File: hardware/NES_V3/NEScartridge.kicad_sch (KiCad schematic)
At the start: 39 parts, among them J1 Conn_02x36_Top_Bottom, U1 TXS0108EPW, U10 TXS0108EPW, U11 TXS0108EPW, U2 TXS0108EPW, U5 TXS0108EPW, U6 TXS0108EPW, U7 TXS0108EPW, U8 TXS0108EPW, U9 TXS0108EPW

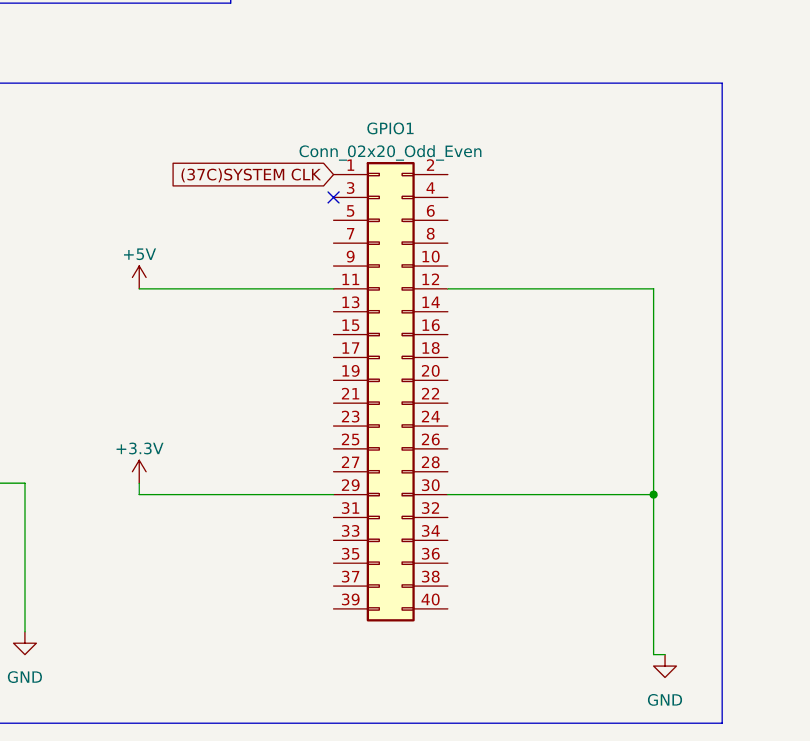
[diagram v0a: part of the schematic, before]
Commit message: Update on the V3 of the cartridge
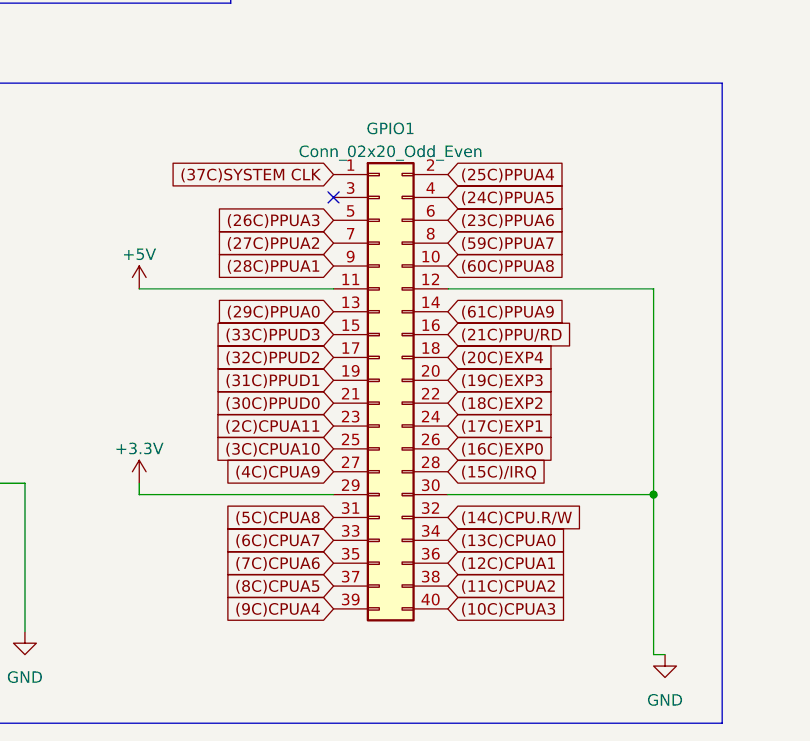
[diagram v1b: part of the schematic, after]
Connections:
- net (10C)CPUA3: now also GPIO1.40 (Pin_40)
- net (11C)CPUA2: now also GPIO1.38 (Pin_38)
- net (12C)CPUA1: now also GPIO1.36 (Pin_36)
- net (13C)CPUA0: now also GPIO1.34 (Pin_34)
- net (14C)CPU.R/W: now also GPIO1.32 (Pin_32)
- net (15C)/IRQ: now also GPIO1.28 (Pin_28)
- net (16C)EXP0: now also GPIO1.26 (Pin_26)
- net (17C)EXP1: now also GPIO1.24 (Pin_24)
- net (18C)EXP2: now also GPIO1.22 (Pin_22)
- net (19C)EXP3: now also GPIO1.20 (Pin_20)
- net (20C)EXP4: now also GPIO1.18 (Pin_18)
- net (21C)PPU/RD: now also GPIO1.16 (Pin_16)
- net (23C)PPUA6: now also GPIO1.6 (Pin_6)
- net (24C)PPUA5: now also GPIO1.4 (Pin_4)
- net (25C)PPUA4: now also GPIO1.2 (Pin_2)
- net (26C)PPUA3: now also GPIO1.5 (Pin_5)
- net (27C)PPUA2: now also GPIO1.7 (Pin_7)
- net (28C)PPUA1: now also GPIO1.9 (Pin_9)
- net (29C)PPUA0: now also GPIO1.13 (Pin_13)
- net (2C)CPUA11: now also GPIO1.23 (Pin_23)
- net (30C)PPUD0: now also GPIO1.21 (Pin_21)
- net (31C)PPUD1: now also GPIO1.19 (Pin_19)
- net (32C)PPUD2: now also GPIO1.17 (Pin_17)
- net (33C)PPUD3: now also GPIO1.15 (Pin_15)
- net (3C)CPUA10: now also GPIO1.25 (Pin_25)
- net (4C)CPUA9: now also GPIO1.27 (Pin_27)
- net (59C)PPUA7: now also GPIO1.8 (Pin_8)
- net (5C)CPUA8: now also GPIO1.31 (Pin_31)
- net (60C)PPUA8: now also GPIO1.10 (Pin_10)
- net (61C)PPUA9: now also GPIO1.14 (Pin_14)
- net (6C)CPUA7: now also GPIO1.33 (Pin_33)
- net (7C)CPUA6: now also GPIO1.35 (Pin_35)
- net (8C)CPUA5: now also GPIO1.37 (Pin_37)
- net (9C)CPUA4: now also GPIO1.39 (Pin_39)

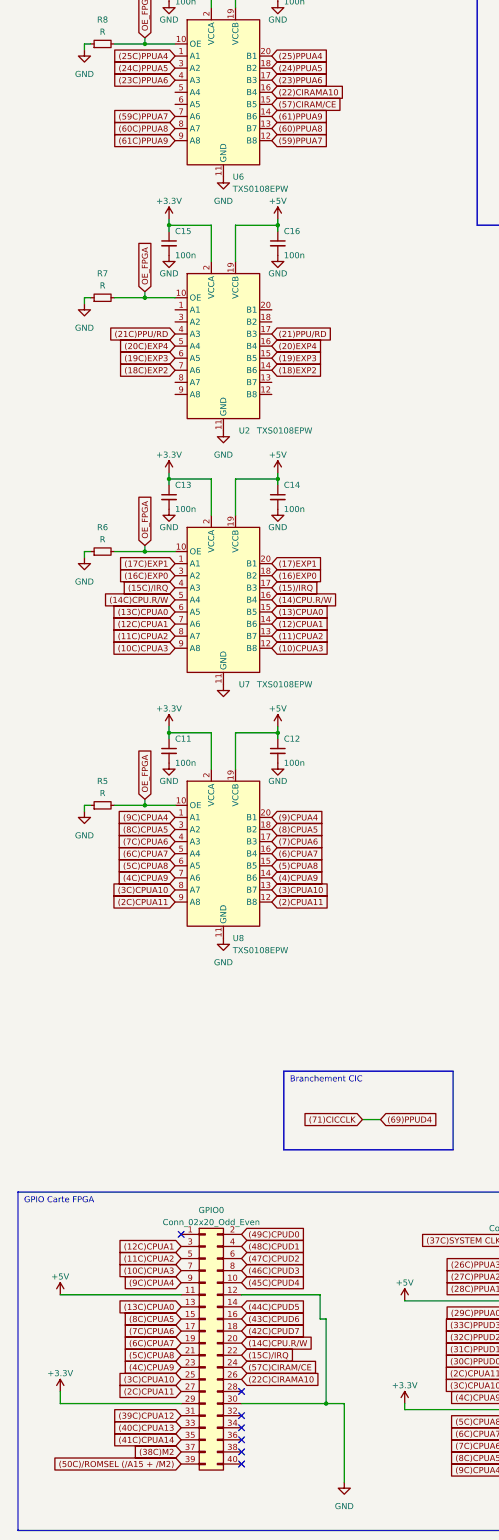
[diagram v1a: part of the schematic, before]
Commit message: Update on the V3 of the cartridge - PCB
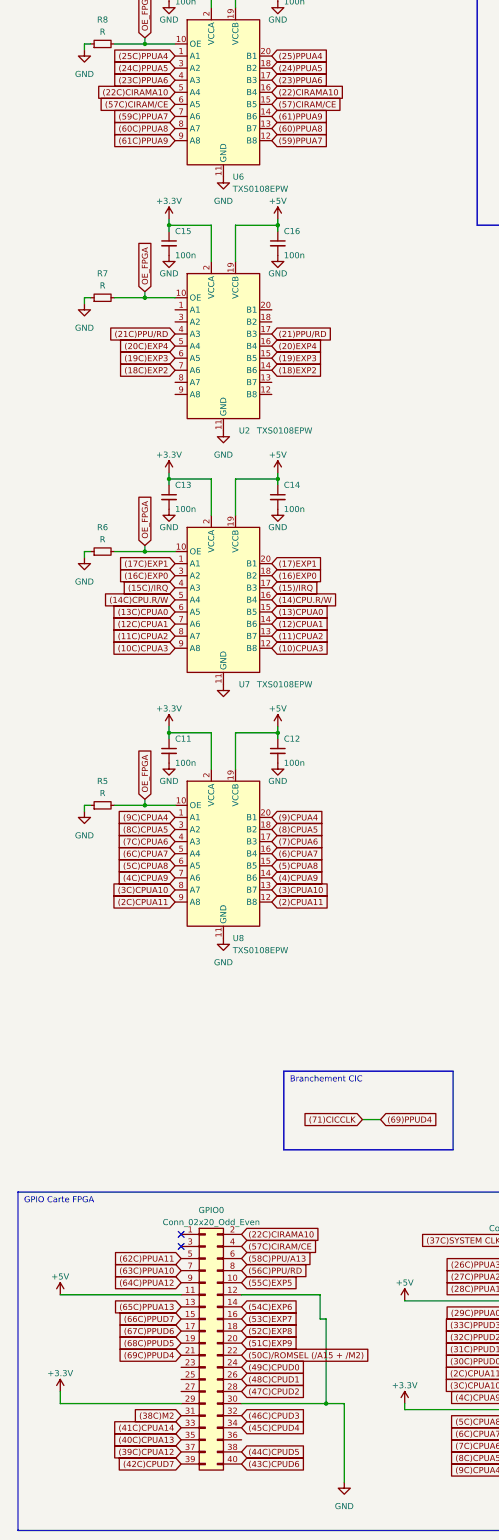
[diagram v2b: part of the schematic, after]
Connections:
- net (10C)CPUA3: no longer GPIO0.7 (Pin_7)
- net (11C)CPUA2: no longer GPIO0.5 (Pin_5)
- net (12C)CPUA1: no longer GPIO0.3 (Pin_3)
- net (13C)CPUA0: no longer GPIO0.13 (Pin_13)
- net (14C)CPU.R/W: no longer GPIO0.20 (Pin_20)
- net (15C)/IRQ: no longer GPIO0.22 (Pin_22)
- net (22C)CIRAMA10: now also GPIO0.2 (Pin_2), U6.5 (A4); no longer GPIO0.26 (Pin_26)
- net (2C)CPUA11: no longer GPIO0.27 (Pin_27)
- net (38C)M2: now also GPIO0.31 (Pin_31); no longer GPIO0.37 (Pin_37)
- net (39C)CPUA12: now also GPIO0.37 (Pin_37); no longer GPIO0.31 (Pin_31)
- net (3C)CPUA10: no longer GPIO0.25 (Pin_25)
- net (40C)CPUA13: now also GPIO0.35 (Pin_35); no longer GPIO0.33 (Pin_33)
- net (41C)CPUA14: now also GPIO0.33 (Pin_33); no longer GPIO0.35 (Pin_35)
- net (42C)CPUD7: now also GPIO0.39 (Pin_39); no longer GPIO0.18 (Pin_18)
- net (43C)CPUD6: now also GPIO0.40 (Pin_40); no longer GPIO0.16 (Pin_16)
- net (44C)CPUD5: now also GPIO0.38 (Pin_38); no longer GPIO0.14 (Pin_14)
- net (45C)CPUD4: now also GPIO0.34 (Pin_34); no longer GPIO0.10 (Pin_10)
- net (46C)CPUD3: now also GPIO0.32 (Pin_32); no longer GPIO0.8 (Pin_8)
- net (47C)CPUD2: now also GPIO0.28 (Pin_28); no longer GPIO0.6 (Pin_6)
- net (48C)CPUD1: now also GPIO0.26 (Pin_26); no longer GPIO0.4 (Pin_4)
- net (49C)CPUD0: now also GPIO0.24 (Pin_24); no longer GPIO0.2 (Pin_2)
- net (4C)CPUA9: no longer GPIO0.23 (Pin_23)
- net (50C)/ROMSEL (/A15 + /M2): now also GPIO0.22 (Pin_22); no longer GPIO0.39 (Pin_39)
- net (51C)EXP9: now also GPIO0.20 (Pin_20)
- net (52C)EXP8: now also GPIO0.18 (Pin_18)
- net (53C)EXP7: now also GPIO0.16 (Pin_16)
- net (54C)EXP6: now also GPIO0.14 (Pin_14)
- net (55C)EXP5: now also GPIO0.10 (Pin_10)
- net (56C)PPU/RD: now also GPIO0.8 (Pin_8)
- net (57C)CIRAM/CE: now also GPIO0.4 (Pin_4), U6.6 (A5); no longer GPIO0.24 (Pin_24)
- net (58C)PPU/A13: now also GPIO0.6 (Pin_6)
- net (5C)CPUA8: no longer GPIO0.21 (Pin_21)
- net (62C)PPUA11: now also GPIO0.5 (Pin_5)
- net (63C)PPUA10: now also GPIO0.7 (Pin_7)
- net (64C)PPUA12: now also GPIO0.9 (Pin_9)
- net (65C)PPUA13: now also GPIO0.13 (Pin_13)
- net (66C)PPUD7: now also GPIO0.15 (Pin_15)
- net (67C)PPUD6: now also GPIO0.17 (Pin_17)
- net (68C)PPUD5: now also GPIO0.19 (Pin_19)
- net (69C)PPUD4: now also GPIO0.21 (Pin_21)
- net (6C)CPUA7: no longer GPIO0.19 (Pin_19)
- net (7C)CPUA6: no longer GPIO0.17 (Pin_17)
- net (8C)CPUA5: no longer GPIO0.15 (Pin_15)
- net (9C)CPUA4: no longer GPIO0.9 (Pin_9)
- no-connect marks 8 -> 3

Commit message: Corrected DRC errors/warning on V5
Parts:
- R10, R11, R12, R13, R5, R6, R7, R8, R9: value R -> 10k
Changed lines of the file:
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@@
     (stroke (width 0) (type default))
   )
-  (polyline (pts (xy 74.93 322.58) (xy 74.93 306.07))
+  (polyline (pts (xy 19.05 328.93) (xy 19.05 312.42))
     (stroke (width 0) (type default))
   )
@@
     (stroke (width 0) (type default))
   )
-  (polyline (pts (xy 74.93 306.07) (xy 110.49 306.07))
+  (polyline (pts (xy 19.05 312.42) (xy 54.61 312.42))
     (stroke (width 0) (type default))
   )
@@
     (stroke (width 0) (type default))
   )
-  (polyline (pts (xy 110.49 322.58) (xy 74.93 322.58))
+  (polyline (pts (xy 54.61 328.93) (xy 19.05 328.93))
     (stroke (width 0) (type default))
   )
@@
     (stroke (width 0) (type default))
   )
-  (wire (pts (xy 91.44 316.23) (xy 95.25 316.23))
+  (wire (pts (xy 35.56 322.58) (xy 39.37 322.58))
     (stroke (width 0) (type default))
   )
@@
     (stroke (width 0) (type default))
   )
-  (polyline (pts (xy 74.93 306.07) (xy 74.93 306.07))
+  (polyline (pts (xy 19.05 312.42) (xy 19.05 312.42))
     (stroke (width 0) (type default))
   )
@@
     (stroke (width 0) (type default))
   )
-  (polyline (pts (xy 110.49 306.07) (xy 110.49 322.58))
+  (polyline (pts (xy 54.61 312.42) (xy 54.61 328.93))
     (stroke (width 0) (type default))
   )
@@
     (effects (font (size 1.27 1.27)) (justify left bottom))
   )
-  (text "Branchement CIC\n" (at 76.2 308.61 0)
+  (text "Branchement CIC\n" (at 20.32 314.96 0)
     (effects (font (size 1.27 1.27)) (justify left bottom))
   )
@@
     )
   )
-  (global_label "(69)PPUD4" (shape input) (at 95.25 316.23 0) (fields_autoplaced)
+  (global_label "(69)PPUD4" (shape input) (at 39.37 322.58 0) (fields_autoplaced)
     (effects (font (size 1.27 1.27) (color 255 0 0 1)) (justify left))
-    (property "Intersheetrefs" "${INTERSHEET_REFS}" (at 108.6182 316.23 0)
+    (property "Intersheetrefs" "${INTERSHEET_REFS}" (at 52.7382 322.58 0)
       (effects (font (size 1.27 1.27)) (justify left) hide)
     )
@@
     )
   )
-  (global_label "(71)CICCLK" (shape input) (at 91.44 316.23 180) (fields_autoplaced)
+  (global_label "(71)CICCLK" (shape input) (at 35.56 322.58 180) (fields_autoplaced)
     (effects (font (size 1.27 1.27)) (justify right))
-    (property "Intersheetrefs" "${INTERSHEET_REFS}" (at 77.6295 316.23 0)
+    (property "Intersheetrefs" "${INTERSHEET_REFS}" (at 21.7495 322.58 0)
       (effects (font (size 1.27 1.27)) (justify right) hide)
     )
@@
       (effects (font (size 1.27 1.27)))
     )
-    (property "Value" "R" (at 36.83 34.29 90)
+    (property "Value" "10k" (at 36.83 34.29 90)
       (effects (font (size 1.27 1.27)))
     )
@@
       (effects (font (size 1.27 1.27)))
     )
-    (property "Value" "R" (at 36.83 194.31 90)
+    (property "Value" "10k" (at 36.83 194.31 90)
       (effects (font (size 1.27 1.27)))
     )
@@
       (effects (font (size 1.27 1.27)))
     )
-    (property "Value" "R" (at 213.36 143.51 90)
+    (property "Value" "10k" (at 213.36 143.51 90)
       (effects (font (size 1.27 1.27)))
     )
@@
       (effects (font (size 1.27 1.27)))
     )
-    (property "Value" "R" (at 213.36 198.12 90)
+    (property "Value" "10k" (at 213.36 198.12 90)
       (effects (font (size 1.27 1.27)))
     )
@@
       (effects (font (size 1.27 1.27)))
     )
-    (property "Value" "R" (at 36.83 247.65 90)
+    (property "Value" "10k" (at 36.83 247.65 90)
       (effects (font (size 1.27 1.27)))
     )
@@
       (effects (font (size 1.27 1.27)))
     )
-    (property "Value" "R" (at 213.36 34.29 90)
+    (property "Value" "10k" (at 213.36 34.29 90)
       (effects (font (size 1.27 1.27)))
     )
@@
       (effects (font (size 1.27 1.27)))
     )
-    (property "Value" "R" (at 213.36 88.9 90)
+    (property "Value" "10k" (at 213.36 88.9 90)
       (effects (font (size 1.27 1.27)))
     )
@@
       (effects (font (size 1.27 1.27)))
     )
-    (property "Value" "R" (at 36.83 87.63 90)
+    (property "Value" "10k" (at 36.83 87.63 90)
       (effects (font (size 1.27 1.27)))
     )
@@
       (effects (font (size 1.27 1.27)))
     )
-    (property "Value" "R" (at 36.83 140.97 90)
+    (property "Value" "10k" (at 36.83 140.97 90)
       (effects (font (size 1.27 1.27)))
     )
